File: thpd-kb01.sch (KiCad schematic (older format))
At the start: 39 parts, among them J1 USB_C_Receptacle_USB2.0, SW1 SW_Push, SW2 SW_SPDT, SW3 Rotary_Encoder_Switch, U1 XC6206PxxxMR, U2 USBLC6-2SC6, U3 NHD-C12832A1Z, U4 STM32F072C8Tx

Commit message: WIP
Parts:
- F1: footprint Fuse:Fuse_1206_3216Metric -> Fuse:Fuse_0603_1608Metric
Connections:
- net ROT_A: now also U4.25 (PB12)
- net ROT_B: now also U4.26 (PB13)
- net led_matrix/DIN: now also U4.12 (PA2)
- net ROW5: now reaches U4.11 (PA1)
- net COL9: now reaches U4.18 (PB0)
- net COL10: now reaches U4.19 (PB1)
- net ROW0: now reaches U4.2 (PC13)
- net COL11: now reaches U4.20 (PB2)
- net COL12: now reaches U4.21 (PB10)
- net COL13: now reaches U4.22 (PB11)
- net COL14: now reaches U4.27 (PB14)
- net COL15: now reaches U4.28 (PB15)
- net COL16: now reaches U4.29 (PA8)
- net ROW1: now reaches U4.3 (PC14)
- net COL17: now reaches U4.30 (PA9)
- net COL18: now reaches U4.31 (PA10)
- net COL0: now reaches U4.37 (PA14)
- net COL1: now reaches U4.38 (PA15)
- net COL2: now reaches U4.39 (PB3)
- net ROW2: now reaches U4.4 (PC15)
- net COL3: now reaches U4.40 (PB4)
- net COL4: now reaches U4.41 (PB5)
- net COL5: now reaches U4.42 (PB6)
- net COL6: now reaches U4.43 (PB7)
- net COL7: now reaches U4.45 (PB8)
- net COL8: now reaches U4.46 (PB9)
- net ROW3: now reaches U4.5 (PF0)
- net ROW4: now reaches U4.6 (PF1)
- no-connect marks 2 -> 4
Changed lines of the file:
@@
 $EndDescr
 $Sheet
-S 6250 3400 550  2550
+S 6200 2400 550  2550
 U 618363D6
 F0 "keys_matrix" 50
 F1 "thpd-kb01-keys.sch" 50
-F2 "ROW0" I L 6250 3450 50
-F3 "ROW1" I L 6250 3550 50
-F4 "ROW2" I L 6250 3650 50
-F5 "ROW3" I L 6250 3750 50
-F6 "ROW4" I L 6250 3850 50
-F7 "ROW5" I L 6250 3950 50
-F8 "COL0" I L 6250 4050 50
-F9 "COL1" I L 6250 4150 50
-F10 "COL2" I L 6250 4250 50
-F11 "COL3" I L 6250 4350 50
-F12 "COL4" I L 6250 4450 50
-F13 "COL5" I L 6250 4550 50
-F14 "COL6" I L 6250 4650 50
-F15 "COL7" I L 6250 4750 50
-F16 "COL8" I L 6250 4850 50
-F17 "COL9" I L 6250 4950 50
-F18 "COL10" I L 6250 5050 50
-F19 "COL11" I L 6250 5150 50
-F20 "COL12" I L 6250 5250 50
-F21 "COL13" I L 6250 5350 50
-F22 "COL14" I L 6250 5450 50
-F23 "COL15" I L 6250 5550 50
-F24 "COL16" I L 6250 5650 50
-F25 "COL17" I L 6250 5750 50
-F26 "COL18" I L 6250 5850 50
+F2 "ROW0" I L 6200 2450 50
+F3 "ROW1" I L 6200 2550 50
+F4 "ROW2" I L 6200 2650 50
+F5 "ROW3" I L 6200 2750 50
+F6 "ROW4" I L 6200 2850 50
+F7 "ROW5" I L 6200 2950 50
+F8 "COL0" I L 6200 3050 50
+F9 "COL1" I L 6200 3150 50
+F10 "COL2" I L 6200 3250 50
+F11 "COL3" I L 6200 3350 50
+F12 "COL4" I L 6200 3450 50
+F13 "COL5" I L 6200 3550 50
+F14 "COL6" I L 6200 3650 50
+F15 "COL7" I L 6200 3750 50
+F16 "COL8" I L 6200 3850 50
+F17 "COL9" I L 6200 3950 50
+F18 "COL10" I L 6200 4050 50
+F19 "COL11" I L 6200 4150 50
+F20 "COL12" I L 6200 4250 50
+F21 "COL13" I L 6200 4350 50
+F22 "COL14" I L 6200 4450 50
+F23 "COL15" I L 6200 4550 50
+F24 "COL16" I L 6200 4650 50
+F25 "COL17" I L 6200 4750 50
+F26 "COL18" I L 6200 4850 50
 $EndSheet
 $Comp
@@
 F 0 "F1" V 5495 1150 50  0000 C CNN
 F 1 "500mA" V 5586 1150 50  0000 C CNN
-F 2 "Fuse:Fuse_1206_3216Metric" H 5750 950 50  0001 L CNN
+F 2 "Fuse:Fuse_0603_1608Metric" H 5750 950 50  0001 L CNN
 F 3 "~" H 5700 1150 50  0001 C CNN
 	1    5700 1150
@@
 $EndComp
 $Sheet
-S 6250 2750 500  300
+S 6200 5200 500  300
 U 625301B3
 F0 "led_matrix" 50
 F1 "thpd-kb01-led.sch" 50
-F2 "DIN" I L 6250 2900 50
+F2 "DIN" I L 6200 5350 50
 $EndSheet
 Text GLabel 1700 7150 3    50   Input ~ 0
@@
 Text GLabel 1500 7150 3    50   Input ~ 0
 ROT_SW_ROW
+Text GLabel 3450 6350 0    50   Input ~ 0
+ROT_A
+Text GLabel 3450 6450 0    50   Input ~ 0
+ROT_B
+Wire Wire Line
+	6200 5350 4750 5350
+Text GLabel 6200 2450 0    50   Input ~ 0
+ROW0
+Text GLabel 6200 2550 0    50   Input ~ 0
+ROW1
+Text GLabel 6200 2650 0    50   Input ~ 0
+ROW2
+Text GLabel 6200 2750 0    50   Input ~ 0
+ROW3
+Text GLabel 6200 2850 0    50   Input ~ 0
+ROW4
+Text GLabel 6200 2950 0    50   Input ~ 0
+ROW5
+Text GLabel 6200 3050 0    50   Input ~ 0
+COL0
+Text GLabel 6200 3150 0    50   Input ~ 0
+COL1
+Text GLabel 6200 3250 0    50   Input ~ 0
+COL2
+Text GLabel 6200 3350 0    50   Input ~ 0
+COL3
+Text GLabel 6200 3450 0    50   Input ~ 0
+COL4
+Text GLabel 6200 3550 0    50   Input ~ 0
+COL5
+Text GLabel 6200 3650 0    50   Input ~ 0
+COL6
+Text GLabel 6200 3750 0    50   Input ~ 0
+COL7
+Text GLabel 6200 3850 0    50   Input ~ 0
+COL8
+Text GLabel 6200 3950 0    50   Input ~ 0
+COL9
+Text GLabel 6200 4050 0    50   Input ~ 0
+COL10
+Text GLabel 6200 4150 0    50   Input ~ 0
+COL11
+Text GLabel 6200 4250 0    50   Input ~ 0
+COL12
+Text GLabel 6200 4350 0    50   Input ~ 0
+COL13
+Text GLabel 6200 4450 0    50   Input ~ 0
+COL14
+Text GLabel 6200 4550 0    50   Input ~ 0
+COL15
+Text GLabel 6200 4650 0    50   Input ~ 0
+COL16
+Text GLabel 6200 4750 0    50   Input ~ 0
+COL17
+Text GLabel 6200 4850 0    50   Input ~ 0
+COL18
+Text GLabel 4750 6550 2    50   Input ~ 0
+COL0
+Text GLabel 4750 6650 2    50   Input ~ 0
+COL1
+Text GLabel 3450 5450 0    50   Input ~ 0
+COL2
+Text GLabel 3450 5550 0    50   Input ~ 0
+COL3
+Text GLabel 3450 5650 0    50   Input ~ 0
+COL4
+Text GLabel 3450 5750 0    50   Input ~ 0
+COL5
+Text GLabel 3450 5850 0    50   Input ~ 0
+COL6
+Text GLabel 3450 5950 0    50   Input ~ 0
+COL7
+Text GLabel 3450 6050 0    50   Input ~ 0
+COL8
+Text GLabel 3450 5150 0    50   Input ~ 0
+COL9
+Text GLabel 3450 5250 0    50   Input ~ 0
+COL10
+Text GLabel 3450 5350 0    50   Input ~ 0
+COL11
+Text GLabel 3450 6150 0    50   Input ~ 0
+COL12
+Text GLabel 3450 6250 0    50   Input ~ 0
+COL13
+Text GLabel 3450 6550 0    50   Input ~ 0
+COL14
+Text GLabel 3450 6650 0    50   Input ~ 0
+COL15
+Text GLabel 4750 5950 2    50   Input ~ 0
+COL16
+Text GLabel 4750 6050 2    50   Input ~ 0
+COL17
+Text GLabel 4750 6150 2    50   Input ~ 0
+COL18
+Text GLabel 3450 4750 0    50   Input ~ 0
+ROW0
+Text GLabel 3450 4850 0    50   Input ~ 0
+ROW1
+Text GLabel 3450 4950 0    50   Input ~ 0
+ROW2
+Text GLabel 3450 4450 0    50   Input ~ 0
+ROW3
+Text GLabel 3450 4550 0    50   Input ~ 0
+ROW4
+Text GLabel 4750 5250 2    50   Input ~ 0
+ROW5
+NoConn ~ 4750 5150
+NoConn ~ 4750 6450
 $EndSCHEMATC

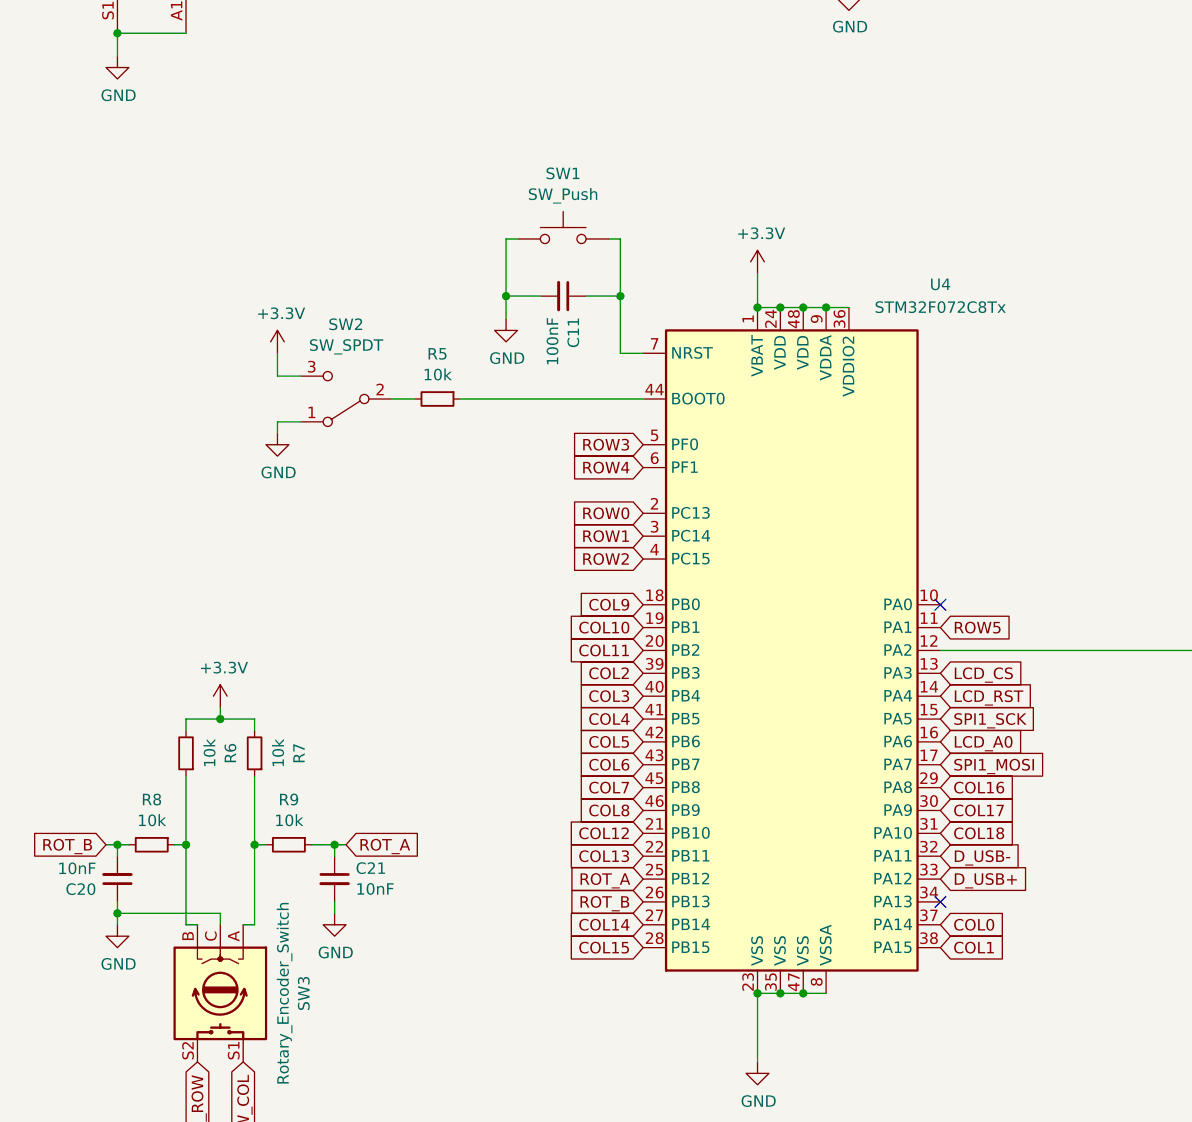
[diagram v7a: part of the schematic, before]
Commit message: Routing of rows and columns done.
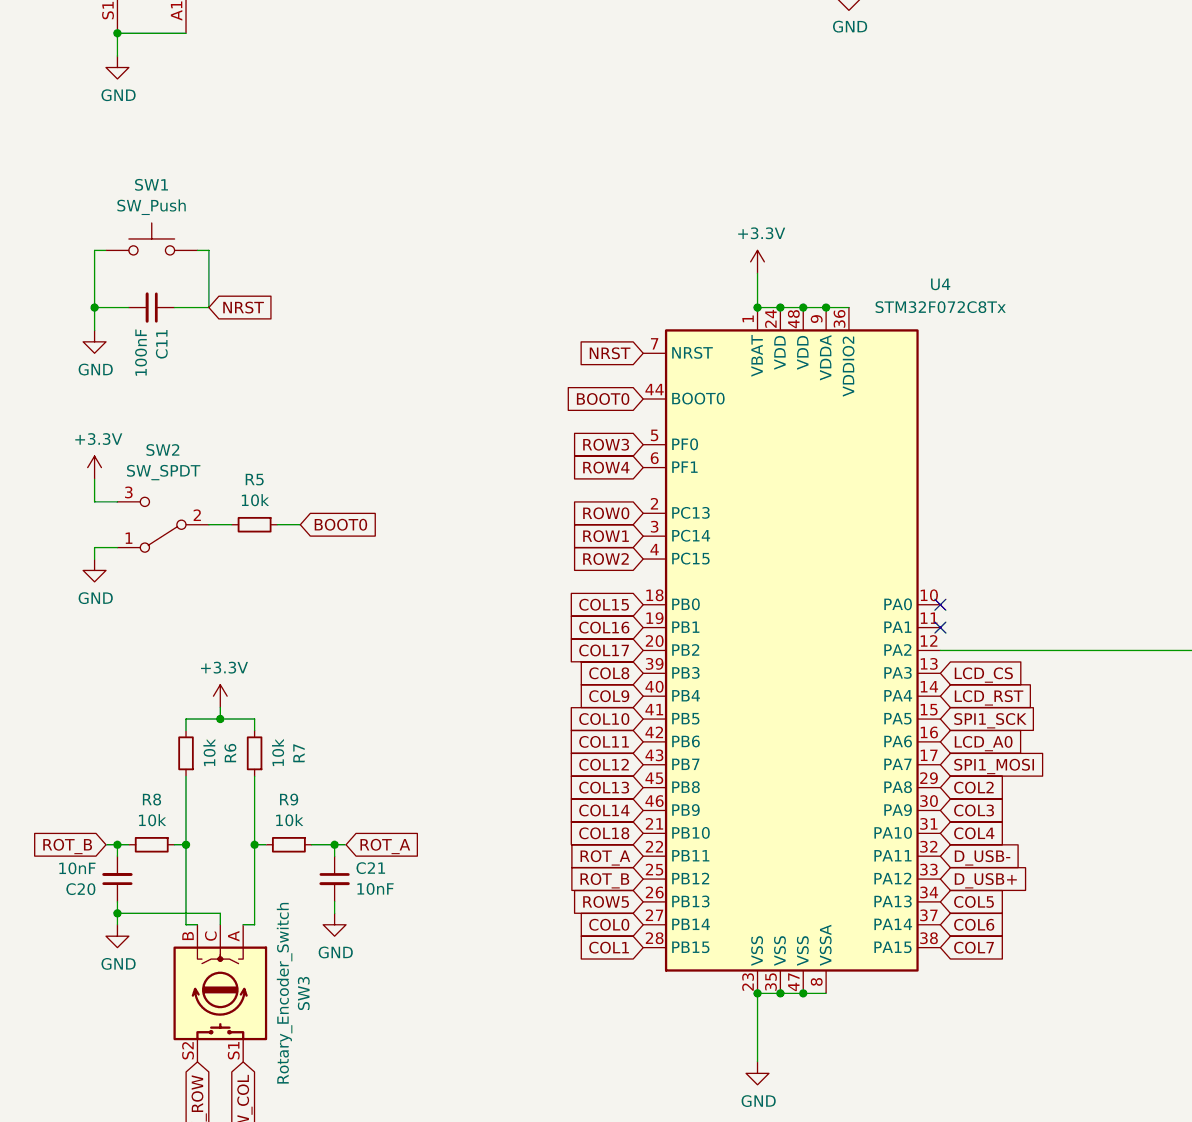
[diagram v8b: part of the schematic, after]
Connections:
- net COL0: now also U4.27 (PB14); no longer U4.37 (PA14)
- net COL1: now also U4.28 (PB15); no longer U4.38 (PA15)
- net COL10: now also U4.41 (PB5); no longer U4.19 (PB1)
- net COL11: now also U4.42 (PB6); no longer U4.20 (PB2)
- net COL12: now also U4.43 (PB7); no longer U4.21 (PB10)
- net COL13: now also U4.45 (PB8); no longer U4.22 (PB11)
- net COL14: now also U4.46 (PB9); no longer U4.27 (PB14)
- net COL15: now also U4.18 (PB0); no longer U4.28 (PB15)
- net COL16: now also U4.19 (PB1); no longer U4.29 (PA8)
- net COL17: now also U4.20 (PB2); no longer U4.30 (PA9)
- net COL18: now also U4.21 (PB10); no longer U4.31 (PA10)
- net COL2: now also U4.29 (PA8); no longer U4.39 (PB3)
- net COL3: now also U4.30 (PA9); no longer U4.40 (PB4)
- net COL4: now also U4.31 (PA10); no longer U4.41 (PB5)
- net COL5: now also U4.34 (PA13); no longer U4.42 (PB6)
- net COL6: now also U4.37 (PA14); no longer U4.43 (PB7)
- net COL7: now also U4.38 (PA15); no longer U4.45 (PB8)
- net COL8: now also U4.39 (PB3); no longer U4.46 (PB9)
- net COL9: now also U4.40 (PB4); no longer U4.18 (PB0)
- net ROT_A: now also U4.22 (PB11); no longer U4.25 (PB12)
- net ROT_B: now also U4.25 (PB12); no longer U4.26 (PB13)
- net ROW5: now also U4.26 (PB13); no longer U4.11 (PA1)
- net BOOT0: now reaches R5.1, U4.44 (BOOT0)
- net NRST: now reaches C11.1, SW1.2, U4.7 (NRST)
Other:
- moved on the sheet: C11, R5, SW1, SW2
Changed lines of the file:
@@
 L power:+3.3V #PWR014
 U 1 1 6193E995
-P 1850 4050
-F 0 "#PWR014" H 1850 3900 50  0001 C CNN
-F 1 "+3.3V" H 1865 4223 50  0000 C CNN
-F 2 "" H 1850 4050 50  0001 C CNN
-F 3 "" H 1850 4050 50  0001 C CNN
-	1    1850 4050
-	1    0    0    -1
-$EndComp
-Wire Wire Line
-	1950 4150 1850 4150
-Wire Wire Line
-	1850 4150 1850 4050
+P 1050 4600
+F 0 "#PWR014" H 1050 4450 50  0001 C CNN
+F 1 "+3.3V" H 1065 4773 50  0000 C CNN
+F 2 "" H 1050 4600 50  0001 C CNN
+F 3 "" H 1050 4600 50  0001 C CNN
+	1    1050 4600
+	1    0    0    -1
+$EndComp
+Wire Wire Line
+	1150 4700 1050 4700
+Wire Wire Line
+	1050 4700 1050 4600
 $Comp
 L power:GND #PWR015
 U 1 1 6193FF44
-P 1850 4400
-F 0 "#PWR015" H 1850 4150 50  0001 C CNN
-F 1 "GND" H 1855 4227 50  0000 C CNN
-F 2 "" H 1850 4400 50  0001 C CNN
-F 3 "" H 1850 4400 50  0001 C CNN
-	1    1850 4400
-	1    0    0    -1
-$EndComp
-Wire Wire Line
-	1950 4350 1850 4350
-Wire Wire Line
-	1850 4350 1850 4400
-$Comp
-L Device:R_Small R5
-U 1 1 61940DE7
-P 2550 4250
-F 0 "R5" V 2354 4250 50  0000 C CNN
-F 1 "10k" V 2445 4250 50  0000 C CNN
-F 2 "Resistor_SMD:R_0603_1608Metric" H 2550 4250 50  0001 C CNN
-F 3 "~" H 2550 4250 50  0001 C CNN
-	1    2550 4250
-	0    1    1    0
-$EndComp
+P 1050 4950
+F 0 "#PWR015" H 1050 4700 50  0001 C CNN
+F 1 "GND" H 1055 4777 50  0000 C CNN
+F 2 "" H 1050 4950 50  0001 C CNN
+F 3 "" H 1050 4950 50  0001 C CNN
+	1    1050 4950
+	1    0    0    -1
+$EndComp
+Wire Wire Line
+	1150 4900 1050 4900
+Wire Wire Line
+	1050 4900 1050 4950
 $Comp
 L Switch:SW_Push SW1
 U 1 1 61942FCD
-P 3100 3550
-F 0 "SW1" H 3100 3835 50  0000 C CNN
-F 1 "SW_Push" H 3100 3744 50  0000 C CNN
-F 2 "Button_Switch_SMD:SW_Push_SPST_NO_Alps_SKRK" H 3100 3750 50  0001 C CNN
-F 3 "~" H 3100 3750 50  0001 C CNN
-	1    3100 3550
+P 1300 3600
+F 0 "SW1" H 1300 3885 50  0000 C CNN
+F 1 "SW_Push" H 1300 3794 50  0000 C CNN
+F 2 "Button_Switch_SMD:SW_Push_SPST_NO_Alps_SKRK" H 1300 3800 50  0001 C CNN
+F 3 "~" H 1300 3800 50  0001 C CNN
+	1    1300 3600
 	1    0    0    -1
 $EndComp
@@
 L power:GND #PWR013
 U 1 1 6194CE67
-P 2850 3900
-F 0 "#PWR013" H 2850 3650 50  0001 C CNN
-F 1 "GND" H 2855 3727 50  0000 C CNN
-F 2 "" H 2850 3900 50  0001 C CNN
-F 3 "" H 2850 3900 50  0001 C CNN
-	1    2850 3900
-	1    0    0    -1
-$EndComp
-Wire Wire Line
-	2650 4250 3450 4250
+P 1050 3950
+F 0 "#PWR013" H 1050 3700 50  0001 C CNN
+F 1 "GND" H 1055 3777 50  0000 C CNN
+F 2 "" H 1050 3950 50  0001 C CNN
+F 3 "" H 1050 3950 50  0001 C CNN
+	1    1050 3950
+	1    0    0    -1
+$EndComp
 $Comp
 L Device:C_Small C11
 U 1 1 619518C0
-P 3100 3800
-F 0 "C11" H 3192 3846 50  0000 L CNN
-F 1 "100nF" H 3192 3755 50  0000 L CNN
-F 2 "Capacitor_SMD:C_0402_1005Metric" H 3100 3800 50  0001 C CNN
-F 3 "~" H 3100 3800 50  0001 C CNN
-	1    3100 3800
+P 1300 3850
+F 0 "C11" H 1392 3896 50  0000 L CNN
+F 1 "100nF" H 1392 3805 50  0000 L CNN
+F 2 "Capacitor_SMD:C_0402_1005Metric" H 1300 3850 50  0001 C CNN
+F 3 "~" H 1300 3850 50  0001 C CNN
+	1    1300 3850
 	0    1    1    0
 $EndComp
 Wire Wire Line
-	3000 3800 2850 3800
-Connection ~ 2850 3800
-Wire Wire Line
-	3450 4050 3350 4050
-Wire Wire Line
-	3350 4050 3350 3800
-Wire Wire Line
-	3200 3800 3350 3800
-Connection ~ 3350 3800
-Wire Wire Line
-	2850 3550 2900 3550
-Wire Wire Line
-	2850 3550 2850 3800
-Wire Wire Line
-	3350 3550 3300 3550
-Wire Wire Line
-	3350 3550 3350 3800
-Wire Wire Line
-	2850 3800 2850 3900
+	1200 3850 1050 3850
+Connection ~ 1050 3850
+Wire Wire Line
+	1400 3850 1550 3850
+Wire Wire Line
+	1050 3600 1100 3600
+Wire Wire Line
+	1050 3600 1050 3850
+Wire Wire Line
+	1550 3600 1500 3600
+Wire Wire Line
+	1550 3600 1550 3850
+Wire Wire Line
+	1050 3850 1050 3950
 $Comp
 L Device:C_Small C3
@@
 $EndComp
 Wire Wire Line
-	2350 4250 2450 4250
+	1550 4800 1650 4800
 $Comp
 L Switch:SW_SPDT SW2
 U 1 1 6193D42E
-P 2150 4250
-F 0 "SW2" H 2150 3925 50  0000 C CNN
-F 1 "SW_SPDT" H 2150 4016 50  0000 C CNN
-F 2 "thpd-kb01-custom:SW_SPDT_K3-1296S-E1" H 2150 4250 50  0001 C CNN
-F 3 "~" H 2150 4250 50  0001 C CNN
-	1    2150 4250
+P 1350 4800
+F 0 "SW2" H 1350 4475 50  0000 C CNN
+F 1 "SW_SPDT" H 1350 4566 50  0000 C CNN
+F 2 "thpd-kb01-custom:SW_SPDT_K3-1296S-E1" H 1350 4800 50  0001 C CNN
+F 3 "~" H 1350 4800 50  0001 C CNN
+	1    1350 4800
 	-1   0    0    1
 $EndComp
@@
 Text GLabel 1500 7150 3    50   Input ~ 0
 ROT_SW_ROW
+Text GLabel 3450 6250 0    50   Input ~ 0
+ROT_A
 Text GLabel 3450 6350 0    50   Input ~ 0
-ROT_A
-Text GLabel 3450 6450 0    50   Input ~ 0
 ROT_B
 Wire Wire Line
@@
 Text GLabel 6200 4850 0    50   Input ~ 0
 COL18
+Text GLabel 3450 6550 0    50   Input ~ 0
+COL0
+Text GLabel 3450 6650 0    50   Input ~ 0
+COL1
+Text GLabel 4750 5950 2    50   Input ~ 0
+COL2
+Text GLabel 4750 6050 2    50   Input ~ 0
+COL3
+Text GLabel 4750 6150 2    50   Input ~ 0
+COL4
+Text GLabel 4750 6450 2    50   Input ~ 0
+COL5
 Text GLabel 4750 6550 2    50   Input ~ 0
-COL0
+COL6
 Text GLabel 4750 6650 2    50   Input ~ 0
-COL1
+COL7
 Text GLabel 3450 5450 0    50   Input ~ 0
-COL2
+COL8
 Text GLabel 3450 5550 0    50   Input ~ 0
-COL3
+COL9
 Text GLabel 3450 5650 0    50   Input ~ 0
-COL4
+COL10
 Text GLabel 3450 5750 0    50   Input ~ 0
-COL5
+COL11
 Text GLabel 3450 5850 0    50   Input ~ 0
-COL6
+COL12
 Text GLabel 3450 5950 0    50   Input ~ 0
-COL7
+COL13
 Text GLabel 3450 6050 0    50   Input ~ 0
-COL8
+COL14
 Text GLabel 3450 5150 0    50   Input ~ 0
-COL9
+COL15
 Text GLabel 3450 5250 0    50   Input ~ 0
-COL10
+COL16
 Text GLabel 3450 5350 0    50   Input ~ 0
-COL11
+COL17
 Text GLabel 3450 6150 0    50   Input ~ 0
-COL12
-Text GLabel 3450 6250 0    50   Input ~ 0
-COL13
-Text GLabel 3450 6550 0    50   Input ~ 0
-COL14
-Text GLabel 3450 6650 0    50   Input ~ 0
-COL15
-Text GLabel 4750 5950 2    50   Input ~ 0
-COL16
-Text GLabel 4750 6050 2    50   Input ~ 0
-COL17
-Text GLabel 4750 6150 2    50   Input ~ 0
 COL18
 Text GLabel 3450 4750 0    50   Input ~ 0
@@
 Text GLabel 3450 4550 0    50   Input ~ 0
 ROW4
-Text GLabel 4750 5250 2    50   Input ~ 0
+Text GLabel 3450 6450 0    50   Input ~ 0
 ROW5
 NoConn ~ 4750 5150
-NoConn ~ 4750 6450
+Text GLabel 1950 4800 2    50   Input ~ 0
+BOOT0
+$Comp
+L Device:R_Small R5
+U 1 1 61940DE7
+P 1750 4800
+F 0 "R5" V 1554 4800 50  0000 C CNN
+F 1 "10k" V 1645 4800 50  0000 C CNN
+F 2 "Resistor_SMD:R_0603_1608Metric" H 1750 4800 50  0001 C CNN
+F 3 "~" H 1750 4800 50  0001 C CNN
+	1    1750 4800
+	0    1    1    0
+$EndComp
+Wire Wire Line
+	1950 4800 1850 4800
+Text GLabel 3450 4250 0    50   Input ~ 0
+BOOT0
+Text GLabel 3450 4050 0    50   Input ~ 0
+NRST
+Text GLabel 1550 3850 2    50   Input ~ 0
+NRST
+NoConn ~ 4750 5250
 $EndSCHEMATC
